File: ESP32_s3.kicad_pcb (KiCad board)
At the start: 2 copper layers, 80 parts, among them J1 Conn_01x02_Pin, J10 TXRX2, J11 backup, J12 Conn_01x02_Pin, J13 Jetson Power Supply, J13 jetsonnano, J14 TXRX, J15 TXRX2, J2 programming header usb, J3 Conn_01x02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

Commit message: update PCB layout
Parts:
- moved J12 198.4 mm to (260.0, 95.5)
- moved J7 192.0 mm to (261.0, 114.0)
- moved J3 191.3 mm to (260.5, 107.5)
- moved J1 190.7 mm to (259.5, 89.5)
- moved D2 151.8 mm to (227.6, 129.1), turned to 90 degrees
- moved R15 151.3 mm to (158.5, 32.4), turned to 90 degrees
- moved D3 149.7 mm to (227.6, 108.6), turned to 90 degrees
- moved U3 146.7 mm to (238.0, 104.3), turned to -90 degrees
- moved D4 145.2 mm to (222.1, 129.7), turned to 90 degrees
- moved D5 144.4 mm to (222.1, 108.6), turned to 90 degrees
- moved R14 144.1 mm to (150.5, 32.9), turned to 90 degrees
- moved D7 139.7 mm to (216.6, 108.9), turned to 90 degrees
- moved D6 138.9 mm to (216.6, 129.6), turned to 90 degrees
- moved J9 138.9 mm to (205.0, 105.5), turned to -90 degrees
- moved J8 136.4 mm to (205.0, 116.0), turned to -90 degrees
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
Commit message: Update PCB Layout
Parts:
- moved J1 20.5 mm to (259.9, 110.0)
- moved J12 20.5 mm to (260.4, 116.0)
- moved C7 20.5 mm to (233.0, 120.7)
- moved D2 20.5 mm to (228.0, 149.6)
- moved D3 20.5 mm to (228.0, 129.1)
- moved D4 20.5 mm to (222.5, 150.2)
- moved D5 20.5 mm to (222.5, 129.1)
- moved D6 20.5 mm to (217.0, 150.1)
- moved D7 20.5 mm to (217.0, 129.4)
- moved D8 20.5 mm to (211.5, 150.4)
- moved D9 20.5 mm to (211.5, 129.4)
- moved J3 20.5 mm to (261.0, 128.0)
- moved J7 20.5 mm to (261.5, 134.5)
- moved J8 20.5 mm to (205.5, 136.5)
- moved J9 20.5 mm to (205.5, 126.0)
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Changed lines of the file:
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@@
 	(footprint "1N5918:DO-41_STM"
 		(layer "F.Cu")
-		(at 216.58 129.6405 90)
+		(at 217.04 150.1405 90)
 		(tags "1N5819 ")
 		(property "Reference" "D6"
@@
 	(footprint "1N5918:DO-41_STM"
 		(layer "F.Cu")
-		(at 227.58 129.1405 90)
+		(at 228.04 149.6405 90)
 		(tags "1N5819 ")
 		(property "Reference" "D2"
@@
 	(footprint "1N5918:DO-41_STM"
 		(layer "F.Cu")
-		(at 227.58 108.6405 90)
+		(at 228.04 129.1405 90)
 		(tags "1N5819 ")
 		(property "Reference" "D3"
@@
 	(footprint "01x02connector:CONN_61300211121_WRE"
 		(layer "F.Cu")
-		(at 261 114)
+		(at 261.46 134.5)
 		(tags "61300211121 ")
 		(property "Reference" "J7"
@@
 	(footprint "01x02connector:CONN_61300211121_WRE"
 		(layer "F.Cu")
-		(at 259.96 95.5)
+		(at 260.42 116)
 		(tags "61300211121 ")
 		(property "Reference" "J12"
@@
 	(footprint "1N5918:DO-41_STM"
 		(layer "F.Cu")
-		(at 222.08 129.735 90)
+		(at 222.54 150.235 90)
 		(tags "1N5819 ")
 		(property "Reference" "D4"
@@
 	(footprint "1N5918:DO-41_STM"
 		(layer "F.Cu")
-		(at 211.08 129.8828 90)
+		(at 211.54 150.3828 90)
 		(tags "1N5819 ")
 		(property "Reference" "D8"
@@
 	(footprint "Package_TO_SOT_THT:TO-220-15_P2.54x2.54mm_StaggerOdd_Lead4.58mm_Vertical"
 		(layer "F.Cu")
-		(at 238 104.34 -90)
+		(at 238.46 124.84 -90)
 		(descr "TO-220-15, Vertical, RM 1.27mm, staggered type-1, see http://www.st.com/resource/en/datasheet/l298.pdf")
 		(tags "TO-220-15 Vertical RM 1.27mm staggered type-1")
@@
 	(footprint "GRM31CC80E227ME11L:CAPC3216X190N"
 		(layer "F.Cu")
-		(at 232.58 100.235 90)
+		(at 233.04 120.735 90)
 		(property "Reference" "C7"
 			(at 3.079 0 180)
@@
 	(footprint "01x02connector:CONN_61300211121_WRE"
 		(layer "F.Cu")
-		(at 205 105.5 -90)
+		(at 205.46 126 -90)
 		(tags "61300211121 ")
 		(property "Reference" "J9"
@@
 	(footprint "1N5918:DO-41_STM"
 		(layer "F.Cu")
-		(at 216.58 108.8828 90)
+		(at 217.04 129.3828 90)
 		(tags "1N5819 ")
 		(property "Reference" "D7"
@@
 	(footprint "01x02connector:CONN_61300211121_WRE"
 		(layer "F.Cu")
-		(at 205 116 -90)
+		(at 205.46 136.5 -90)
 		(tags "61300211121 ")
 		(property "Reference" "J8"
@@
 	(footprint "01x02connector:CONN_61300211121_WRE"
 		(layer "F.Cu")
-		(at 259.46 89.5)
+		(at 259.92 110)
 		(tags "61300211121 ")
 		(property "Reference" "J1"
@@
 	(footprint "01x02connector:CONN_61300211121_WRE"
 		(layer "F.Cu")
-		(at 260.5 107.5)
+		(at 260.96 128)
 		(tags "61300211121 ")
 		(property "Reference" "J3"
@@
 	(footprint "1N5918:DO-41_STM"
 		(layer "F.Cu")
-		(at 222.08 108.6405 90)
+		(at 222.54 129.1405 90)
 		(tags "1N5819 ")
 		(property "Reference" "D5"
@@
 	(footprint "1N5918:DO-41_STM"
 		(layer "F.Cu")
-		(at 211.08 108.8828 90)
+		(at 211.54 129.3828 90)
 		(tags "1N5819 ")
 		(property "Reference" "D9"

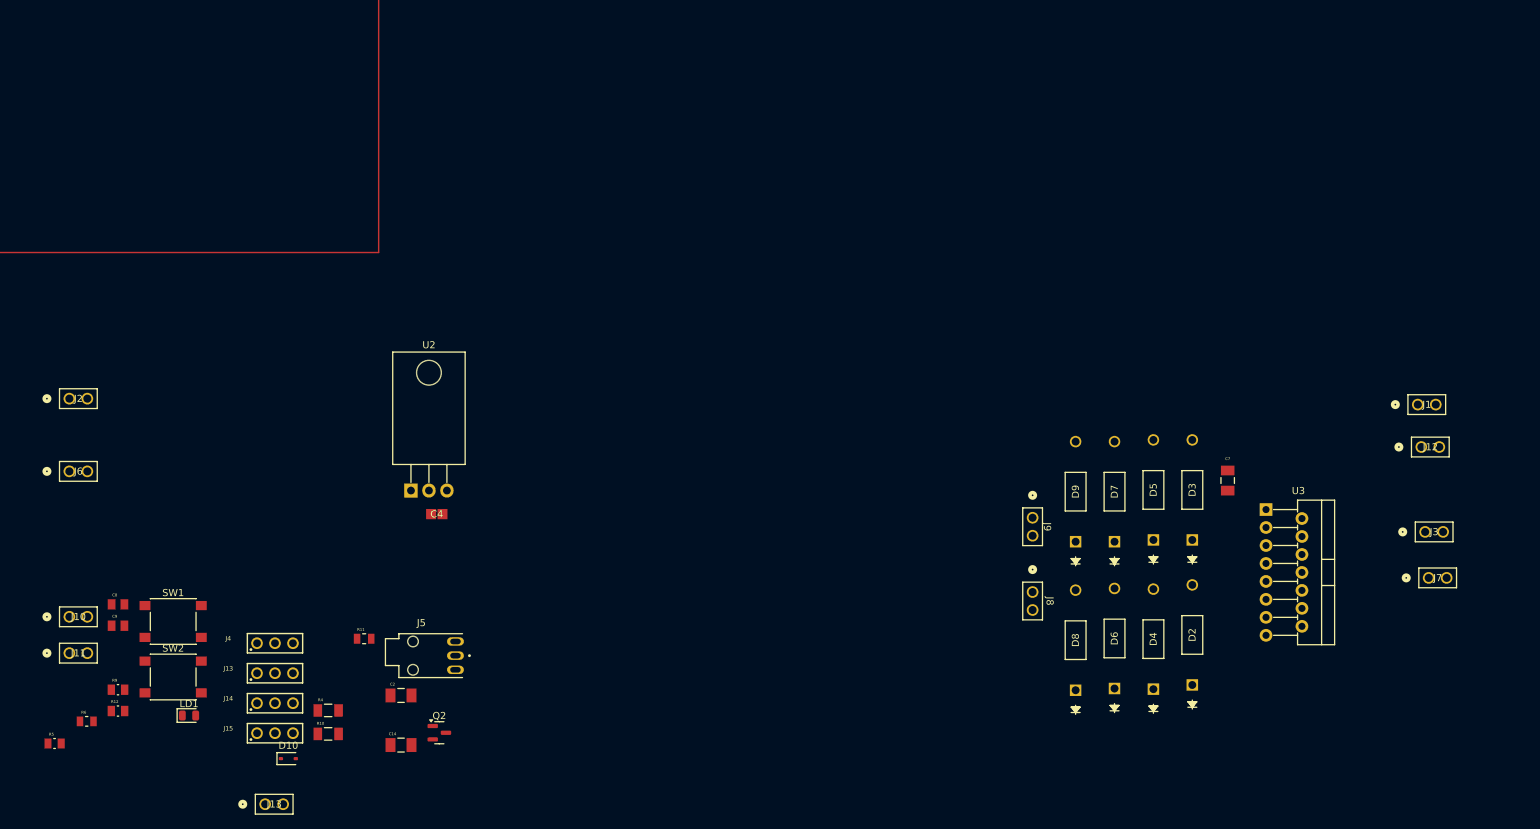
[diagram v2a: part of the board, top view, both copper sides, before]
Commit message: PCB layout done (need traces)
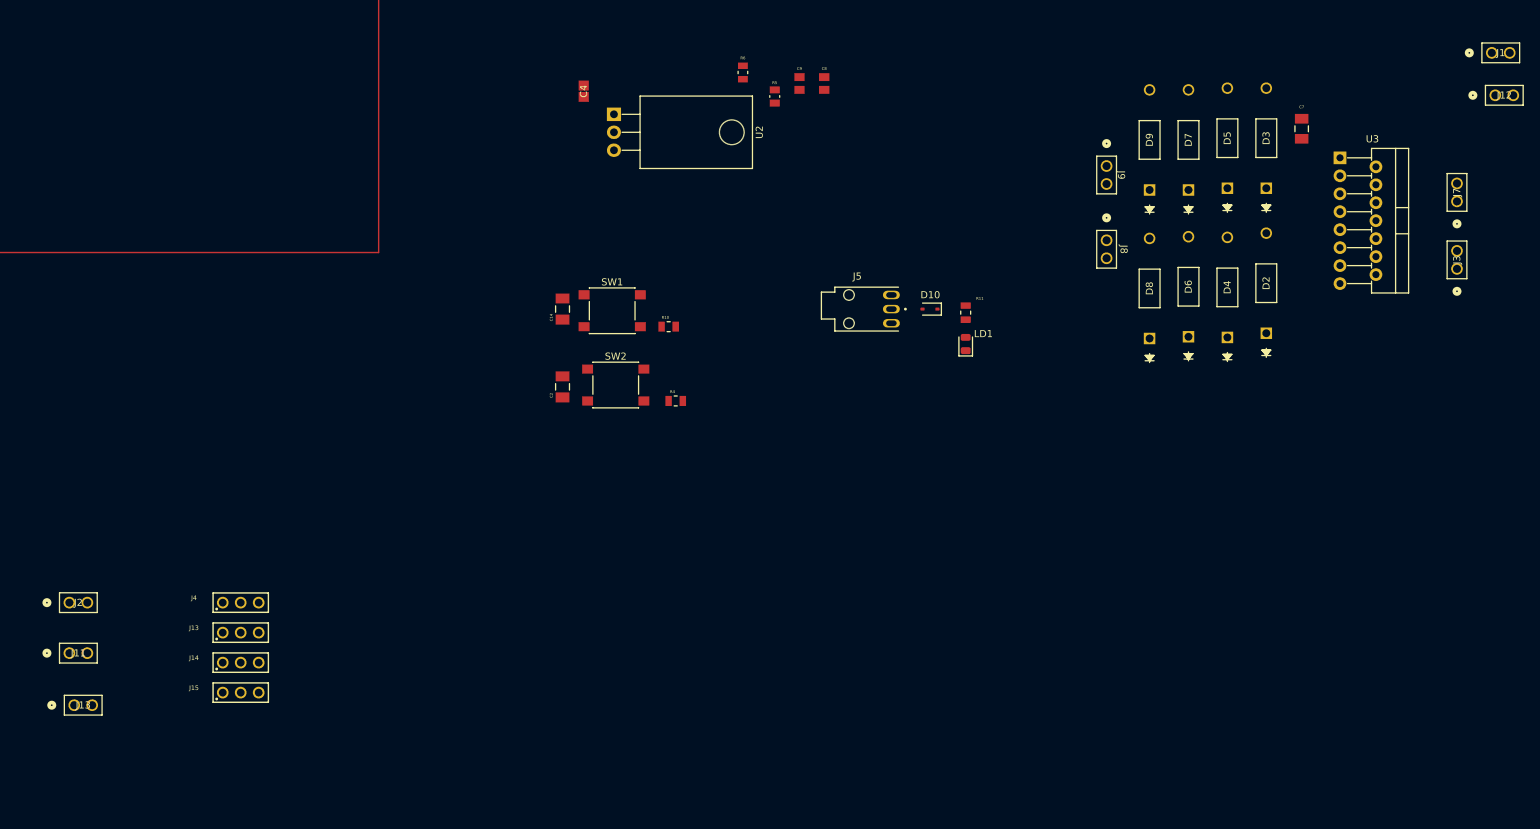
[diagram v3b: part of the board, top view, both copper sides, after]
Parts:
- removed J10: TXRX2, 01x02connector:CONN_61300211121_WRE
- removed J6: TXRX, 01x02connector:CONN_61300211121_WRE
- removed Q2: BSS138, Package_TO_SOT_SMD:SOT-23
- removed R12, R9: 10000, RR1220P-1030-D:RESC2012X50N
- R10, R4: value 0 -> 10k; footprint RMCF1206ZR0R00:RESC3216X70N -> CRCW080535K7FKEA:RESC2012X50N
- moved R5 136.9 mm to (169.0, 66.4), turned to 90 degrees
- moved R6 130.5 mm to (164.5, 63.0), turned to 90 degrees
- moved C8 124.1 mm to (176.0, 64.6), turned to 90 degrees
- moved C9 123.1 mm to (172.5, 64.6), turned to 90 degrees
- moved LD1 121.7 mm to (196.0, 101.4), turned to 90 degrees
- moved D10 110.8 mm to (190.9, 96.5), turned to 180 degrees
- moved R11 96.7 mm to (196.0, 97.0), turned to -90 degrees
- moved J5 78.7 mm to (185.5, 96.5)
- moved SW1 76.0 mm to (146.0, 96.7)
- moved R10 75.0 mm to (154.0, 99.0)
- moved SW2 75.0 mm to (146.5, 107.2)
- moved R4 65.8 mm to (155.0, 109.5)
- moved C14 65.7 mm to (139.0, 96.5), turned to 90 degrees
- moved C4 63.3 mm to (142.0, 65.7), turned to 90 degrees
- moved U2 60.4 mm to (146.3, 69.0), turned to -90 degrees
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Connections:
- C14 pad 1: +3.3V -> /EN
- C2 pad 1: +3.3V -> /GPIO0
- R10 pad 1: +3.3V -> /EN
- R10 pad 2: /EN -> +3.3V
- R4 pad 1: +3.3V -> /GPIO0
- R4 pad 2: /GPIO0 -> +3.3V
- SW1 pad 2: +3.3V -> /EN
- SW2 pad 2: +3.3V -> /GPIO0

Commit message: small fix of connector and LM1117 footprint
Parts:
- removed J1, J12: Conn_01x02_Pin, 01x02connector:CONN_61300211121_WRE
- removed J2: programming header usb, 01x02connector:CONN_61300211121_WRE
- U2: footprint Package_TO_SOT_THT:TO-220-3_Horizontal_TabDown -> LM1117T-ADJ:TO254P1054X470X1955-3
- moved Cbst1 207.9 mm to (49.5, 75.9)
- moved Ccomp1 207.9 mm to (60.0, 70.9)
- moved Ccomp2 207.9 mm to (64.0, 70.5)
- moved Cin1 207.9 mm to (38.0, 79.8)
- moved Cin2 207.9 mm to (42.0, 79.5)
- moved Cout1 207.9 mm to (58.0, 78.0)
- moved Css1 207.9 mm to (51.5, 81.0)
- moved Cvcc1 207.9 mm to (49.5, 67.0)
- moved DbLED1 207.9 mm to (45.5, 82.4)
- moved DrLED1 207.9 mm to (63.0, 80.9)
- moved L1 207.9 mm to (43.4, 71.9)
- moved RbLED1 207.9 mm to (45.5, 77.9)
- moved Rcomp1 207.9 mm to (63.0, 73.9)
- moved Rfbb1 207.9 mm to (67.0, 73.9)
- moved Rfbt1 207.9 mm to (70.8, 74.9)
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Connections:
- net /GPIO10 renamed GPIO10
- net /GPIO11 renamed GPIO11
- net /GPIO12 renamed GPIO12
- net /GPIO9 renamed GPIO9

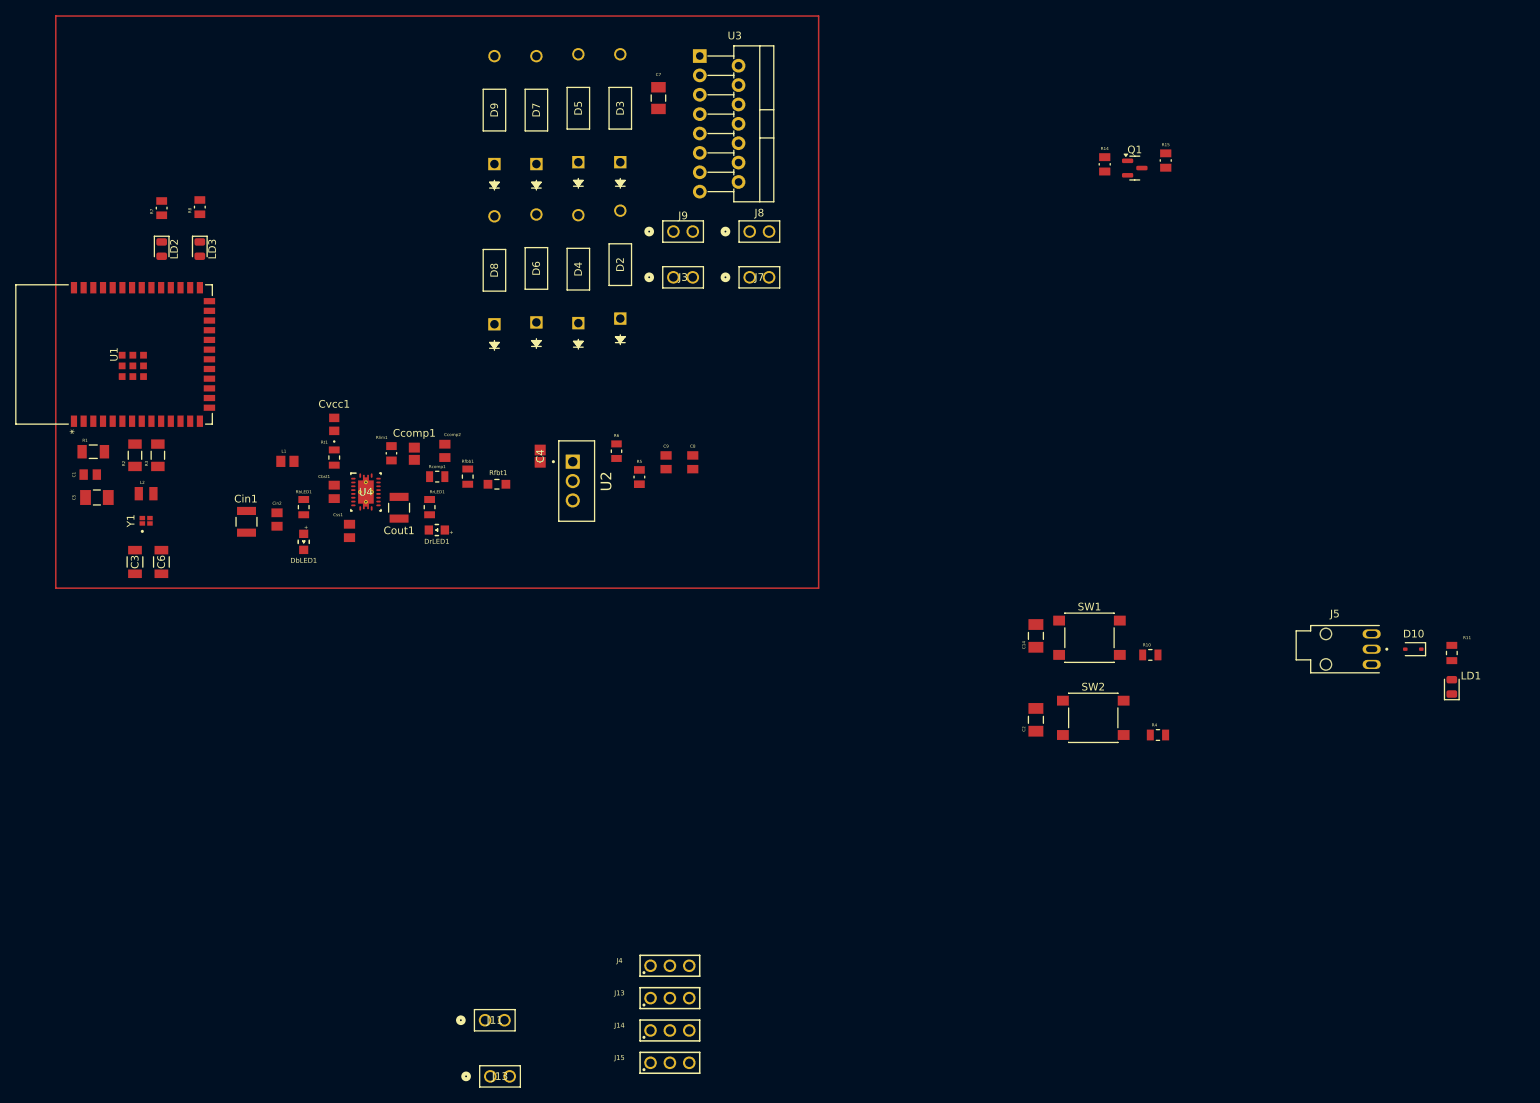
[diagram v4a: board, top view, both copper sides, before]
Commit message: complete PCB layout in region
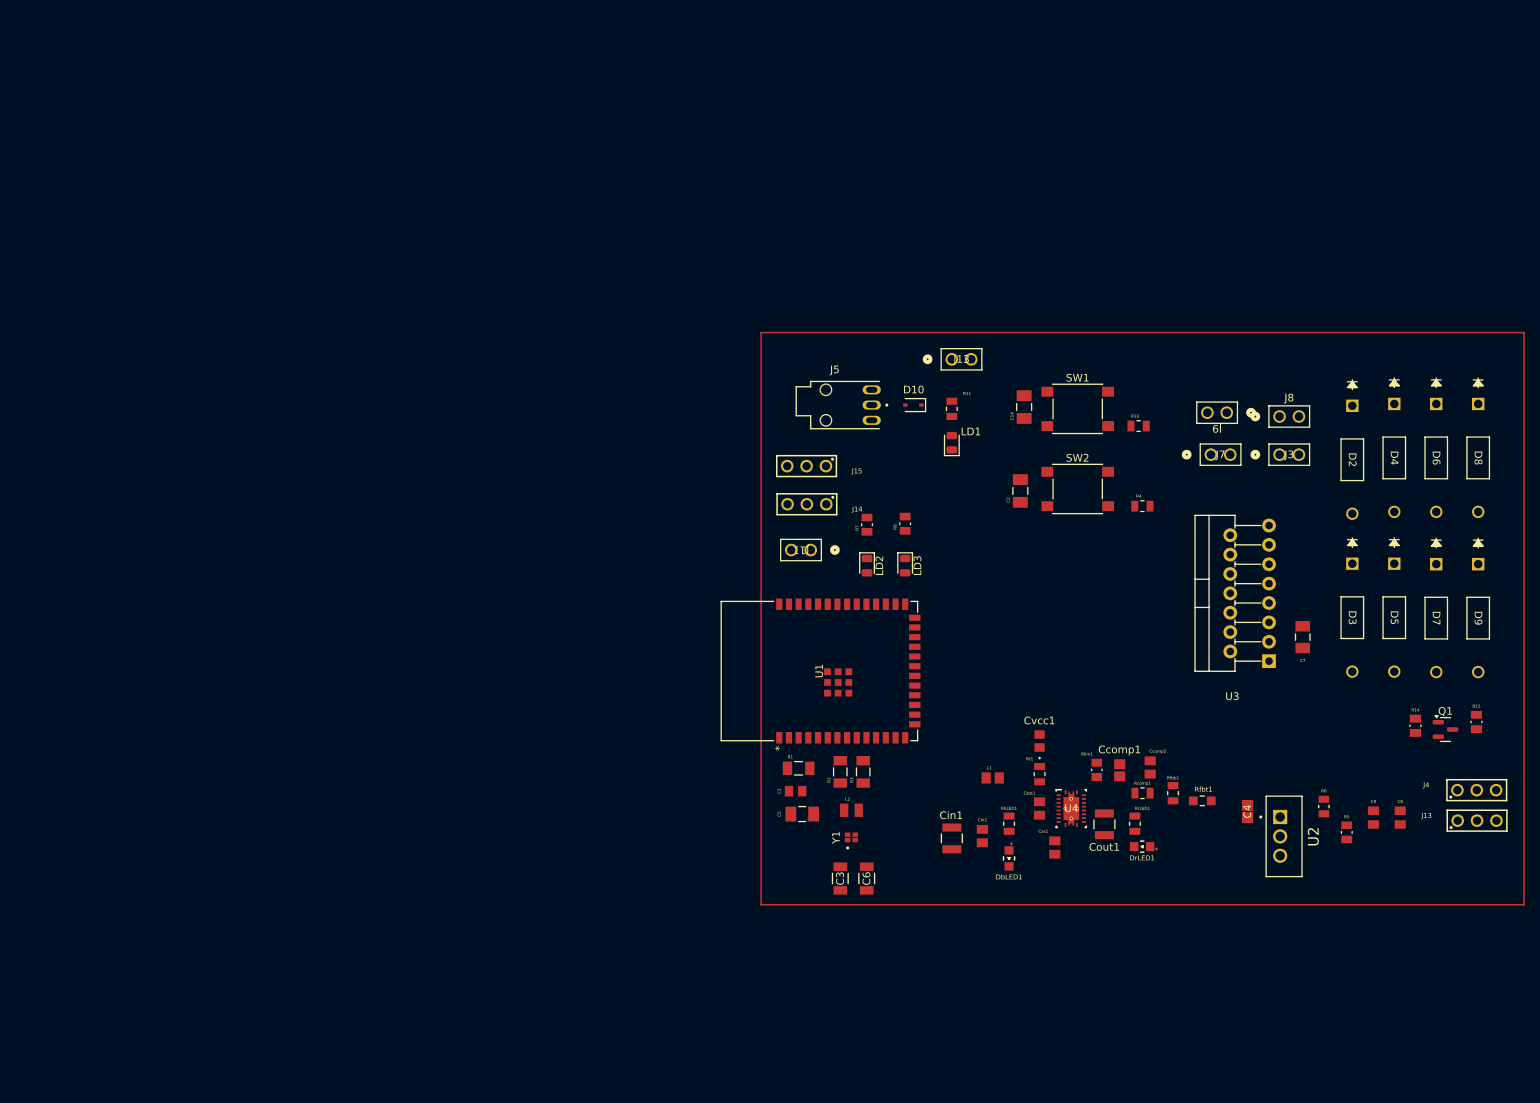
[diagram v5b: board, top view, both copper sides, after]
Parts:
- moved D9 139.2 mm to (199.5, 85.4), turned to -90 degrees
- moved D8 129.4 mm to (199.5, 64.4), turned to -90 degrees
- moved D7 129.1 mm to (194.0, 85.4), turned to -90 degrees
- moved D5 119.2 mm to (188.5, 85.3), turned to -90 degrees
- moved D6 118.4 mm to (194.0, 64.4), turned to -90 degrees
- moved J13 111.8 mm to (130.5, 58.5)
- moved C7 110.1 mm to (176.5, 94.9), turned to -90 degrees
- moved D3 109.4 mm to (183.0, 85.3), turned to -90 degrees
- moved U3 108.9 mm to (172.0, 98.1), turned to 90 degrees
- moved J13 108.3 mm to (199.3, 119.0)
- moved J4 108.2 mm to (199.3, 115.0)
- moved D4 107.5 mm to (188.5, 64.4), turned to -90 degrees
- moved U2 103.8 mm to (173.5, 121.0)
- moved C4 103.8 mm to (169.2, 117.8)
- moved C8 103.8 mm to (189.2, 118.6)
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
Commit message: add a few traces
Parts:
- moved C14 23.2 mm to (143.0, 87.8)
- moved C2 23.2 mm to (142.5, 98.8)
- moved R10 23.2 mm to (158.0, 90.2)
- moved R4 23.2 mm to (158.5, 100.8)
- moved SW1 23.2 mm to (150.0, 88.0)
- moved SW2 23.2 mm to (150.0, 98.5)
- moved J7 20.0 mm to (144.5, 70.0)
- moved J3 18.4 mm to (155.0, 70.0)
- moved R8 16.0 mm to (135.0, 92.0)
- moved LD2 16.0 mm to (130.0, 97.4)
- moved LD3 16.0 mm to (135.0, 97.4)
- moved R7 16.0 mm to (130.0, 92.1)
- moved J11 14.8 mm to (126.5, 86.5)
- moved J8 8.94 mm to (165.0, 63.0)
- moved J15 8.55 mm to (110.5, 81.0)
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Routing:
- net GND: track 0.00 -> 252.6 mm
- net /EN: track 0.00 -> 63.4 mm
- net +12V: track 0.00 -> 58.3 mm
- net +5V: track 0.00 -> 53.5 mm
- net /GPIO38: track 0.00 -> 36.0 mm
- net +3.3V: track 0.00 -> 31.4 mm
- net /GPIO48: track 0.00 -> 21.8 mm
- net Vout: track 0.00 -> 17.7 mm
- net /TXD0: track 0.00 -> 17.4 mm
- net Vin: track 0.00 -> 15.8 mm
- net /GPIO0: track 0.00 -> 15.2 mm
- net Net-(U4-FB): track 0.00 -> 14.5 mm
- net /GPIO41: track 0.00 -> 13.0 mm
- net Net-(C6-Pad2): track 0.00 -> 12.6 mm
- net Net-(C3-Pad2): track 0.00 -> 12.3 mm
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
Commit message: update trace
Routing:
- net Net-(D8-A): track 0.00 -> 59.1 mm
- net Net-(J7-Pin_1): track 0.00 -> 31.5 mm
- net Net-(D2-A): track 0.00 -> 29.8 mm
- net Net-(D4-A): track 0.00 -> 27.5 mm
- net Net-(D6-A): track 0.00 -> 26.7 mm
- net Net-(J3-Pin_1): track 0.00 -> 25.7 mm
- net GND: track 252.6 -> 264.5 mm
- net Net-(J3-Pin_2): track 0.00 -> 11.5 mm

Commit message: update traces
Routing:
- net +3.3V: track 31.4 -> 141.4 mm, vias 0 -> 4
- net GND: track 264.5 -> 351.1 mm, vias 0 -> 7
- net /GPIO13: track 3.21 -> 72.7 mm, vias 0 -> 2
- net GPIO9: track 0.00 -> 59.0 mm
- net GPIO10: track 0.00 -> 57.7 mm
- net GPIO11: track 0.00 -> 52.3 mm, vias 0 -> 2
- net GPIO12: track 0.00 -> 51.4 mm, vias 0 -> 2
- net Net-(D2-A): track 29.8 -> 77.6 mm
- net +5V: track 53.5 -> 88.6 mm, vias 0 -> 3
- net Net-(D4-A): track 27.5 -> 61.0 mm
- net /GPIO0: track 15.2 -> 42.5 mm, vias 0 -> 2
- net Net-(D6-A): track 26.7 -> 49.6 mm, vias 0 -> 1
- net Net-(Cbst1-Pad2): track 5.19 -> 12.2 mm
- net Vin: track 15.8 -> 22.1 mm
- net /TXD0: track 17.4 -> 19.2 mm
